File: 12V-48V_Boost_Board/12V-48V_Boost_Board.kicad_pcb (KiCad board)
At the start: 2 copper layers, 65.1 x 76.7 mm, 42 parts, among them J1 12V Input, J2 Input Current Sensing, J3 Output Current Sensing, J4 48V Output, J5 Output Measuring, Q1 FDWS86068-F085, U2 INA290

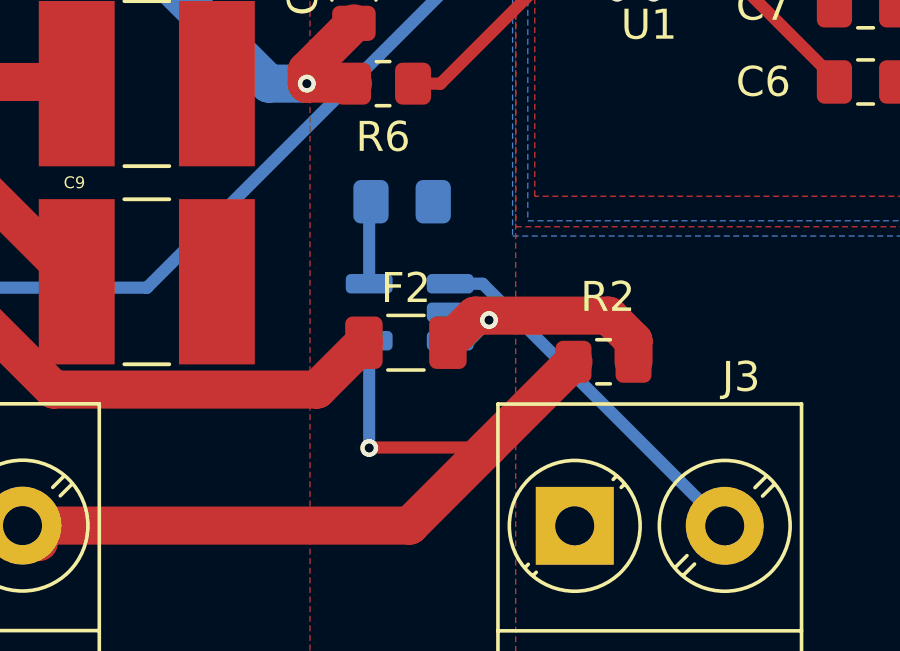
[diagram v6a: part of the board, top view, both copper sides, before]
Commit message: Updated INA290 symbol and footprint
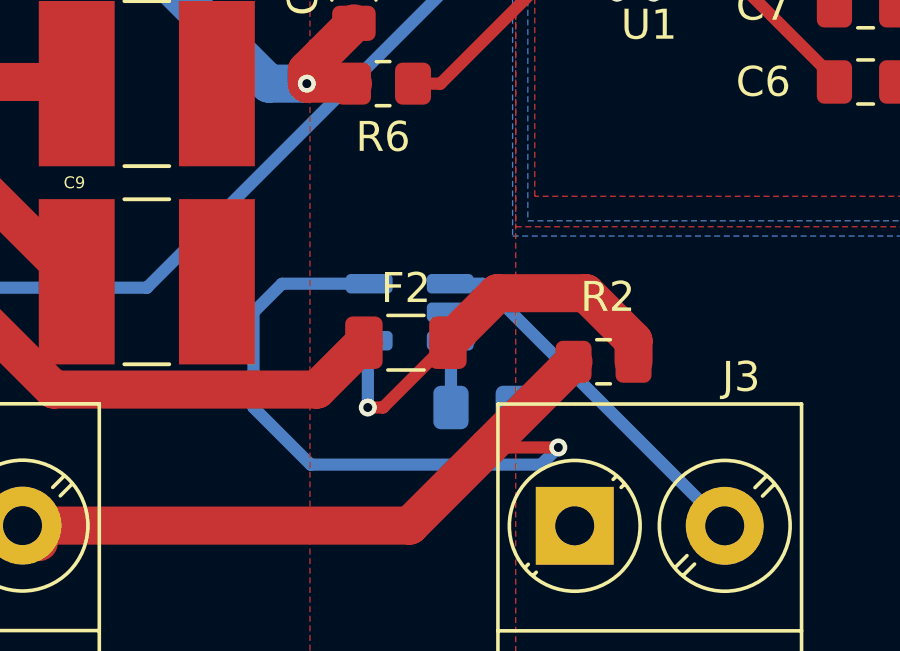
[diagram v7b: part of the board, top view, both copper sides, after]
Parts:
- moved C13 7.36 mm to (149.9, 135.3)
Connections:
- U2 pad 3: Net-(U2-IN+) -> +5V
- U2 pad 4: Net-(J4-Pin_2) -> Net-(U2-IN+)
- U2 pad 5: +5V -> Net-(J4-Pin_2)
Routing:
- net Net-(J4-Pin_2): track 38.5 -> 52.0 mm
- net Net-(U2-IN+): track 10.9 -> 14.0 mm
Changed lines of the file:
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@@
 			)
 		)
-		(property "Datasheet" "http://www.ti.com/lit/ds/symlink/ina180.pdf"
+		(property "Datasheet" "https://www.ti.com/lit/ds/symlink/ina290.pdf"
 			(at 0 0 0)
 			(unlocked yes)
@@
 			(layers "B.Cu" "B.Paste" "B.Mask")
 			(roundrect_rratio 0.25)
+			(net 22 "+5V")
+			(pinfunction "VS")
+			(pintype "power_in")
+		)
+		(pad "4" smd roundrect
+			(at 1.35 -0.95 180)
+			(size 1.56 0.65)
+			(layers "B.Cu" "B.Paste" "B.Mask")
+			(roundrect_rratio 0.25)
 			(net 23 "Net-(U2-IN+)")
 			(pinfunction "IN+")
 			(pintype "input")
 		)
-		(pad "4" smd roundrect
-			(at 1.35 -0.95 180)
+		(pad "5" smd roundrect
+			(at 1.35 0.95 180)
 			(size 1.56 0.65)
 			(layers "B.Cu" "B.Paste" "B.Mask")
@@
 			(pinfunction "IN-")
 			(pintype "input")
-		)
-		(pad "5" smd roundrect
-			(at 1.35 0.95 180)
-			(size 1.56 0.65)
-			(layers "B.Cu" "B.Paste" "B.Mask")
-			(roundrect_rratio 0.25)
-			(net 22 "+5V")
-			(pinfunction "VS")
-			(pintype "power_in")
 		)
 		(model "${KICAD8_3DMODEL_DIR}/Package_TO_SOT_SMD.3dshapes/SOT-23-5.wrl"
@@
 	(footprint "Capacitor_SMD:C_0805_2012Metric_Pad1.18x1.45mm_HandSolder"
 		(layer "B.Cu")
-		(at 147.193 128.397 180)
+		(at 149.86 135.255 180)
 		(descr "Capacitor SMD 0805 (2012 Metric), square (rectangular) end terminal, IPC_7351 nominal with elongated pad for handsoldering. (Body size source: IPC-SM-782 page 76, https://www.pcb-3d.com/wordpress/wp-content/uploads/ipc-sm-782a_amendment_1_and_2.pdf, https://docs.google.com/spreadsheets/d/1BsfQQcO9C6DZCsRaXUlFlo91Tg2WpOkGARC1WS5S8t0/edit?usp=sharing), generated with kicad-footprint-generator")
 		(tags "capacitor handsolder")
@@
 	)
 	(segment
-		(start 146.097 128.4555)
-		(end 146.1555 128.397)
+		(start 148.8225 135.255)
+		(end 148.8225 133.0555)
 		(width 0.4064)
 		(layer "B.Cu")
@@
 	)
 	(segment
-		(start 146.097 131.13)
-		(end 146.097 128.4555)
+		(start 149.43605 133.03)
+		(end 148.797 133.03)
 		(width 0.4064)
 		(layer "B.Cu")
@@
 	)
 	(segment
-		(start 149.3378 133.096)
+		(start 148.8225 133.0555)
+		(end 148.797 133.03)
+		(width 0.4064)
+		(layer "B.Cu")
+		(net 22)
+	)
+	(segment
+		(start 153.322 131.445)
+		(end 154.908 133.031)
+		(width 1.27)
+		(layer "F.Cu")
+		(net 23)
+	)
+	(segment
+		(start 146.05 135.255)
+		(end 146.561 135.255)
+		(width 0.4064)
+		(layer "F.Cu")
+		(net 23)
+	)
+	(segment
+		(start 150.371 131.445)
+		(end 153.322 131.445)
+		(width 1.27)
+		(layer "F.Cu")
+		(net 23)
+	)
+	(segment
+		(start 146.561 135.255)
 		(end 148.72 133.096)
 		(width 0.4064)
@@
 	)
 	(segment
-		(start 150.091399 132.342401)
-		(end 149.3378 133.096)
-		(width 0.4064)
+		(start 148.72 133.096)
+		(end 150.371 131.445)
+		(width 1.27)
 		(layer "F.Cu")
 		(net 23)
 	)
-	(segment
-		(start 148.72 133.096)
-		(end 149.6232 132.1928)
-		(width 1.27)
-		(layer "F.Cu")
-		(net 23)
-	)
-	(segment
-		(start 154.0698 132.1928)
-		(end 154.908 133.031)
-		(width 1.27)
-		(layer "F.Cu")
-		(net 23)
-	)
-	(segment
-		(start 149.6232 132.1928)
-		(end 154.0698 132.1928)
-		(width 1.27)
-		(layer "F.Cu")
-		(net 23)
-	)
 	(via
-		(at 150.091399 132.342401)
+		(at 146.05 135.255)
 		(size 0.6)
 		(drill 0.3)
@@
 	)
 	(segment
-		(start 150.091399 132.342401)
-		(end 150.091399 132.374651)
+		(start 146.05 135.255)
+		(end 146.05 133.077)
 		(width 0.4064)
 		(layer "B.Cu")
@@
 	)
 	(segment
-		(start 149.43605 133.03)
-		(end 148.797 133.03)
+		(start 146.05 133.077)
+		(end 146.097 133.03)
 		(width 0.4064)
 		(layer "B.Cu")
 		(net 23)
-	)
-	(segment
-		(start 150.091399 132.374651)
-		(end 149.43605 133.03)
-		(width 0.4064)
-		(layer "B.Cu")
-		(net 23)
-	)
-	(segment
-		(start 146.097 136.605)
-		(end 146.1135 136.5885)
-		(width 0.4064)
-		(layer "F.Cu")
-		(net 24)
 	)
 	(segment
@@
 	)
 	(segment
-		(start 146.1135 136.5885)
-		(end 150.0505 136.5885)
-		(width 0.4064)
-		(layer "F.Cu")
-		(net 24)
-	)
-	(segment
 		(start 134.54 139.192)
 		(end 133.572 139.192)
@@
 		(net 24)
 	)
+	(segment
+		(start 152.4 136.5885)
+		(end 150.0505 136.5885)
+		(width 0.4064)
+		(layer "F.Cu")
+		(net 24)
+	)
 	(via
-		(at 146.097 136.605)
+		(at 152.4 136.5885)
 		(size 0.6)
 		(drill 0.3)
@@
 	)
 	(segment
-		(start 146.097 133.03)
-		(end 146.097 136.605)
-		(width 0.4064)
-		(layer "B.Cu")
+		(start 146.097 131.13)
+		(end 143.19 131.13)
+		(width 0.4064)
+		(layer "B.Cu")
+		(net 24)
+	)
+	(segment
+		(start 142.24 132.08)
+		(end 142.24 135.255)
+		(width 0.4064)
+		(layer "B.Cu")
+		(net 24)
+	)
+	(segment
+		(start 143.19 131.13)
+		(end 142.24 132.08)
+		(width 0.4064)
+		(layer "B.Cu")
+		(net 24)
+	)
+	(segment
+		(start 144.145 137.16)
+		(end 151.8285 137.16)
+		(width 0.4064)
+		(layer "B.Cu")
+		(net 24)
+	)
+	(segment
+		(start 142.24 135.255)
+		(end 144.145 137.16)
+		(width 0.4064)
+		(layer "B.Cu")
+		(net 24)
+	)
+	(segment
+		(start 151.8285 137.16)
+		(end 152.4 136.5885)
+		(width 0.4064)
+		(layer "B.Cu")

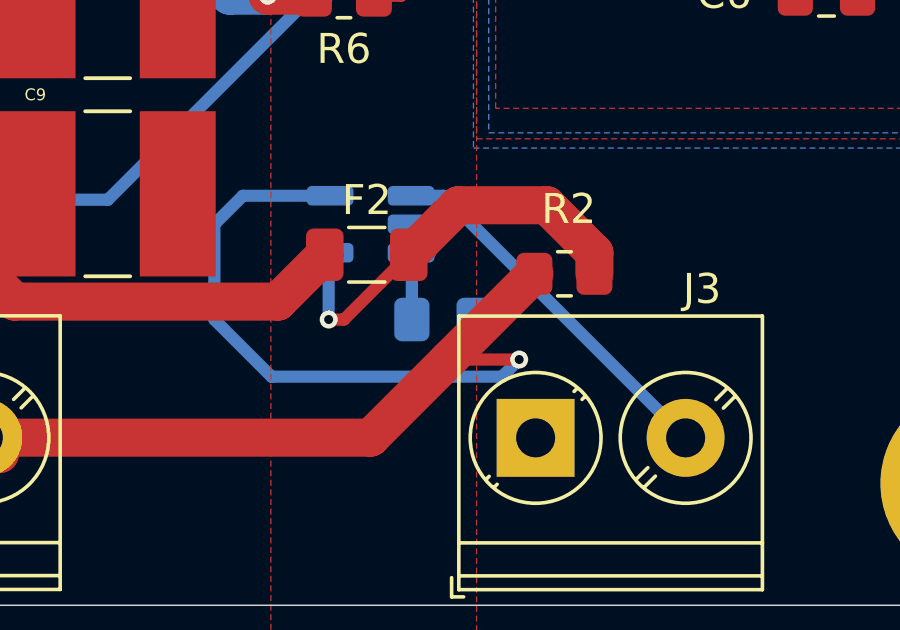
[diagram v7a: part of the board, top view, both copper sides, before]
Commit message: Actually updated INA290 footprint
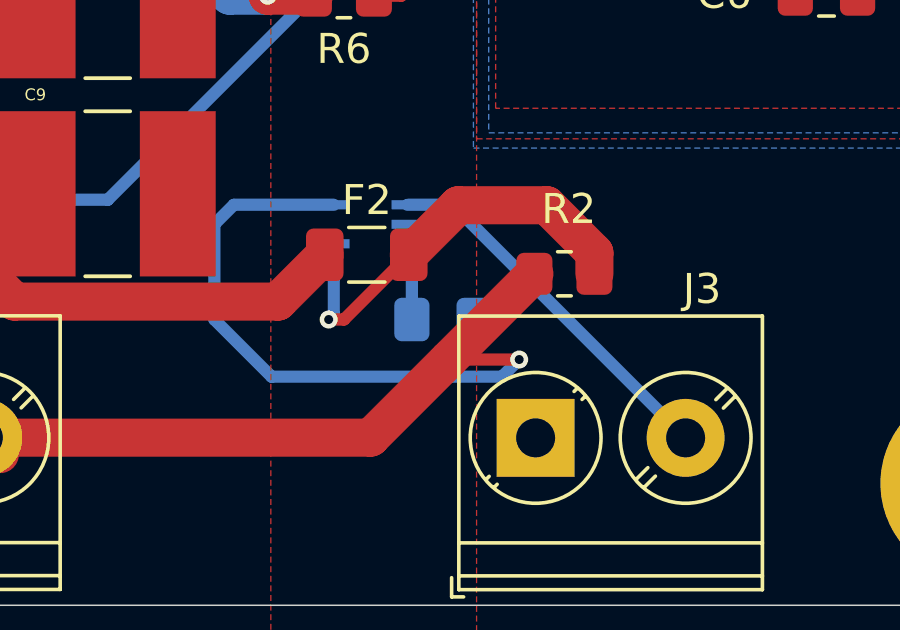
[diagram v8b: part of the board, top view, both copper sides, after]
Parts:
- U2: footprint Package_TO_SOT_SMD:SOT-23-5_HandSoldering -> 12/48 boost:SC70-5_DCK_TEX
